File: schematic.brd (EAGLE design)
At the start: 160 x 100 mm, 91 parts, among them J1 MEGAFIT-4SKT-RA, J10 JST-PA-SMT-RA-4, J11 JST-PA-SMT-RA-2, J12 JST-PA-SMT-RA-2, J14 JST-PA-SMT-RA-2, J15 JST-PA-SMT-RA-2, J17 JST-PA-SMT-RA-3, J18 JST-PA-SMT-RA-3, J19 JST-PA-SMT-RA-4, J20 JST-PA-SMT-RA-4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

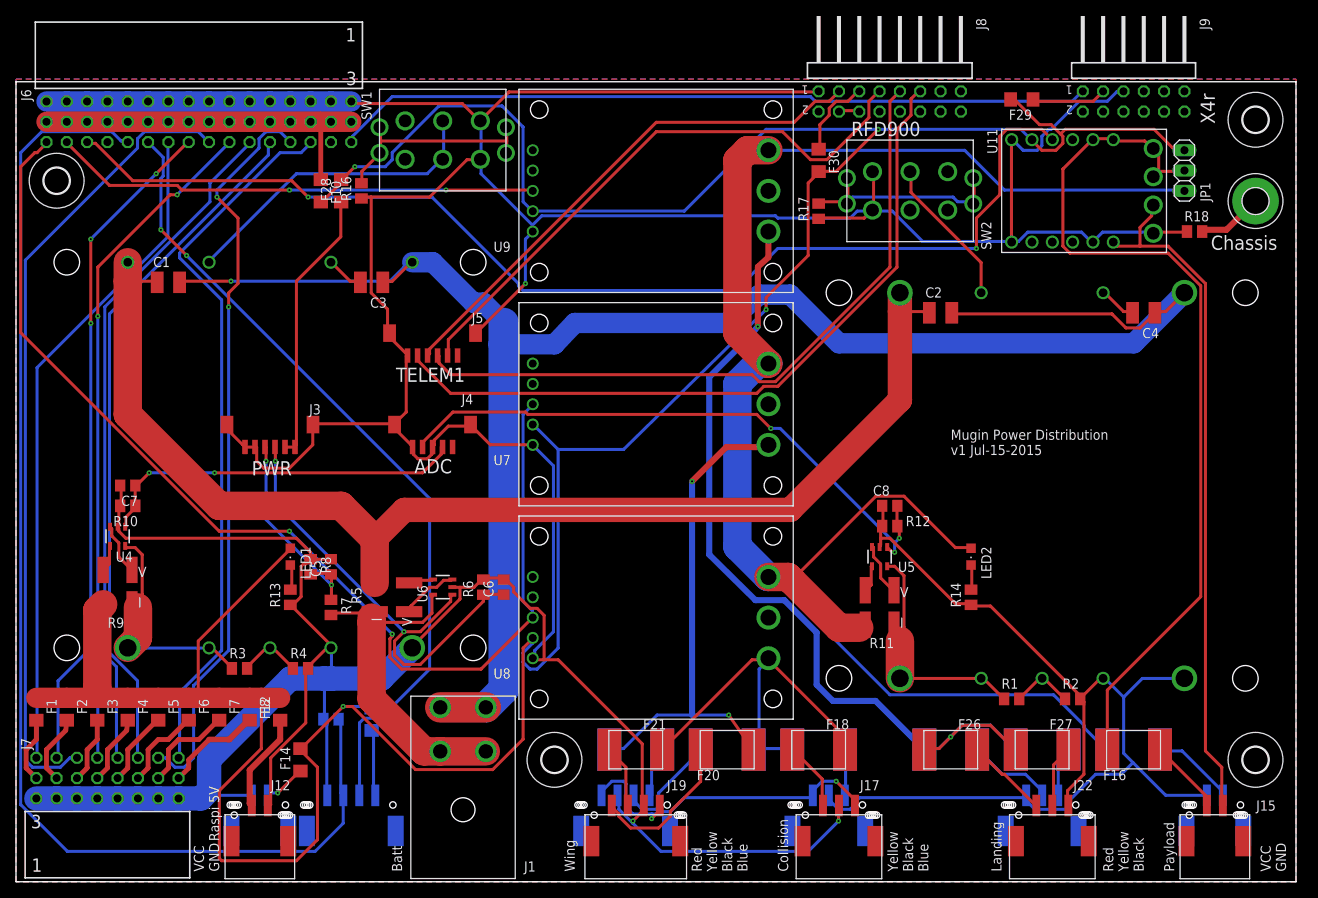
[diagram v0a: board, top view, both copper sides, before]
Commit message: Rotating pixhawk so the df13 connectors on that board and on top.  Autorouting signals after flipping.
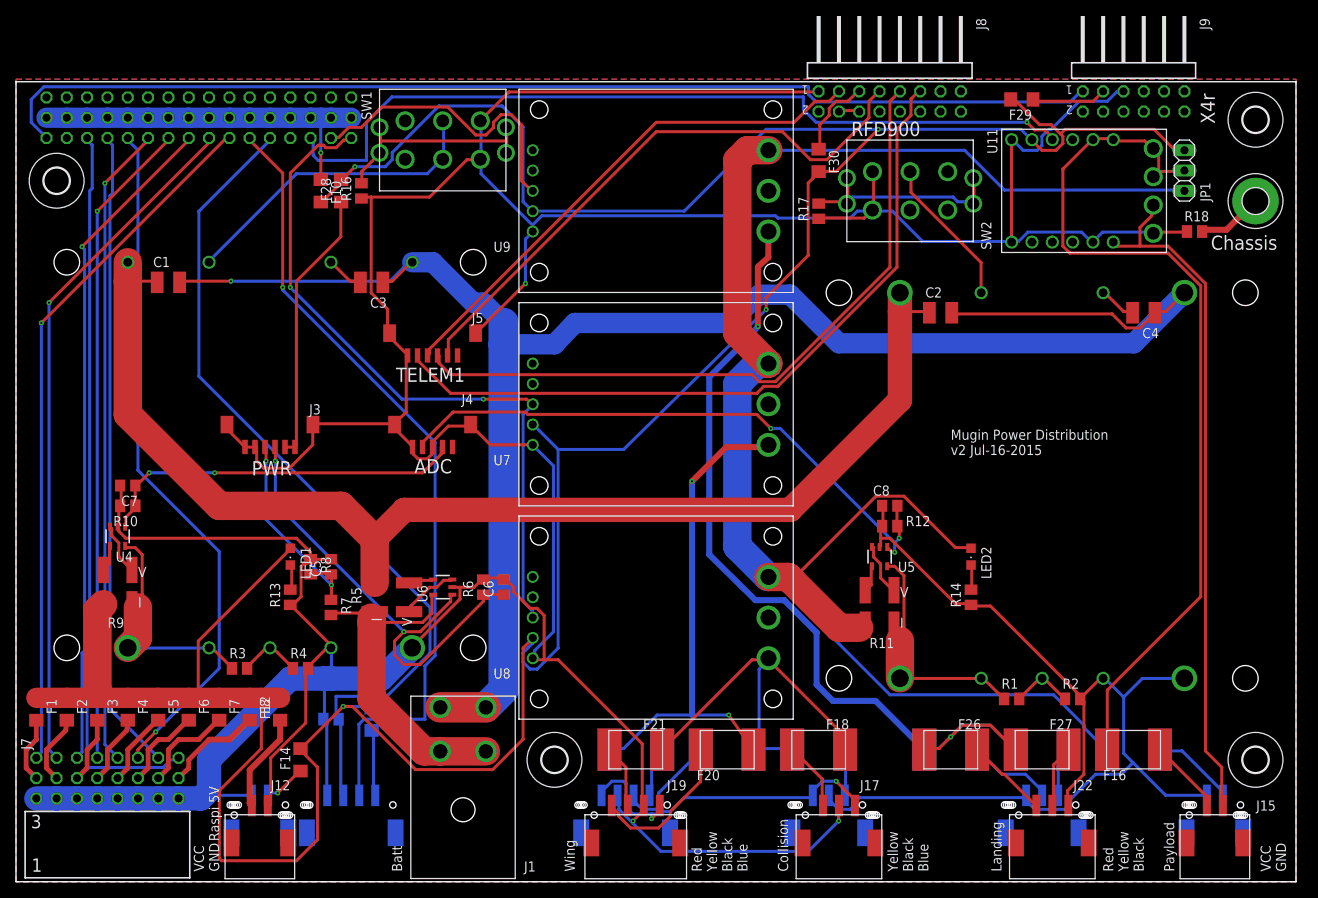
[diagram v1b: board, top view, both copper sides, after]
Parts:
- moved J6 0.51 mm to (22.9, 99.6), flipped to the bottom
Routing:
- net GND: track 773.6 -> 718.1 mm
- net AUX1: track 139.2 -> 88.1 mm
- net AUX5: track 154.0 -> 107.0 mm
- net RC_SIG: track 94.9 -> 140.0 mm
- net AUX3: track 143.9 -> 104.3 mm, vias 2 -> 1
- net AUX2: track 60.8 -> 37.8 mm, vias 2 -> 0
- net MAIN3: track 100.6 -> 83.5 mm, vias 0 -> 1
- net MAIN7: track 93.2 -> 80.4 mm, vias 2 -> 0
- net MAIN5: track 85.1 -> 80.4 mm, vias 0 -> 1
- net MAIN1: track 83.8 -> 87.8 mm, vias 0 -> 1
- net MAIN4: track 84.3 -> 81.2 mm, vias 2 -> 1
- net MAIN2: track 83.8 -> 86.1 mm, vias 3 -> 1
- net MAIN8: track 89.7 -> 91.5 mm
- net AUX6: track 101.3 -> 100.2 mm, vias 2 -> 1
- net N$5: track 45.3 -> 45.8 mm, vias 0 -> 1
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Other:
- board text added: "Mugin Power Distribution v2 Jul-16-2015"
- board text removed: "Mugin Power Distribution v1 Jul-15-2015"
